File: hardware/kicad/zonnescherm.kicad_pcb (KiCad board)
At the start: 2 copper layers, 75 x 75 mm, 33 parts, among them K1 K1-ON/OFF, K2 K1-UP/DOWN, K3 K2-ON/OFF, K4 K2-UP/DOWN, P1 ARDUINO-ISP, P2 CONN_MAINS, P3 CONN_SUNSHADE1, P4 CONN_SUNSHADE2, P5 SWITCHES, U1 IRM-05-5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

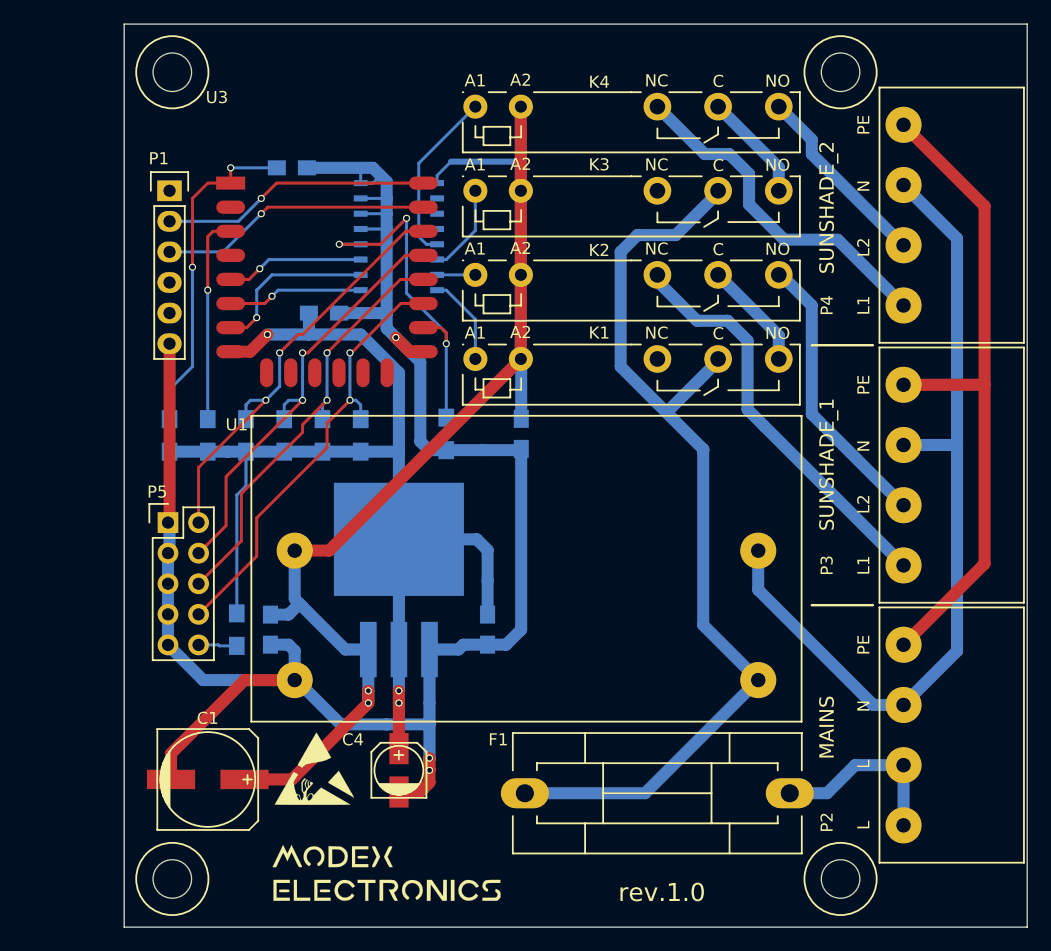
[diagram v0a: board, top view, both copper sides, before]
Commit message: Updated layout with new footprint.
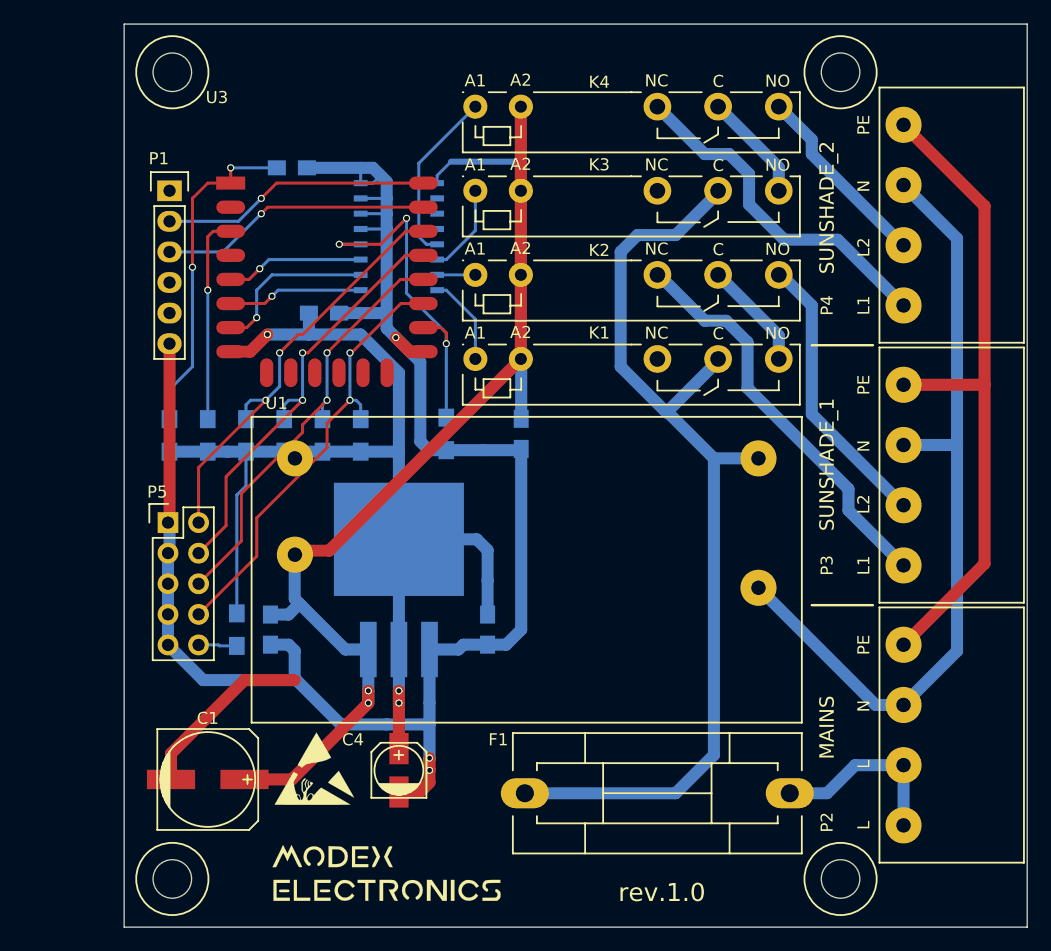
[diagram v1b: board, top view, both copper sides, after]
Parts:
- moved U1 42.7 mm to (122.7, 95.0), turned to 0 degrees
- moved ? 7.37 mm to (153.2, 100.1)
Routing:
- net N: track 70.8 -> 67.6 mm
- net P: track 80.3 -> 82.3 mm

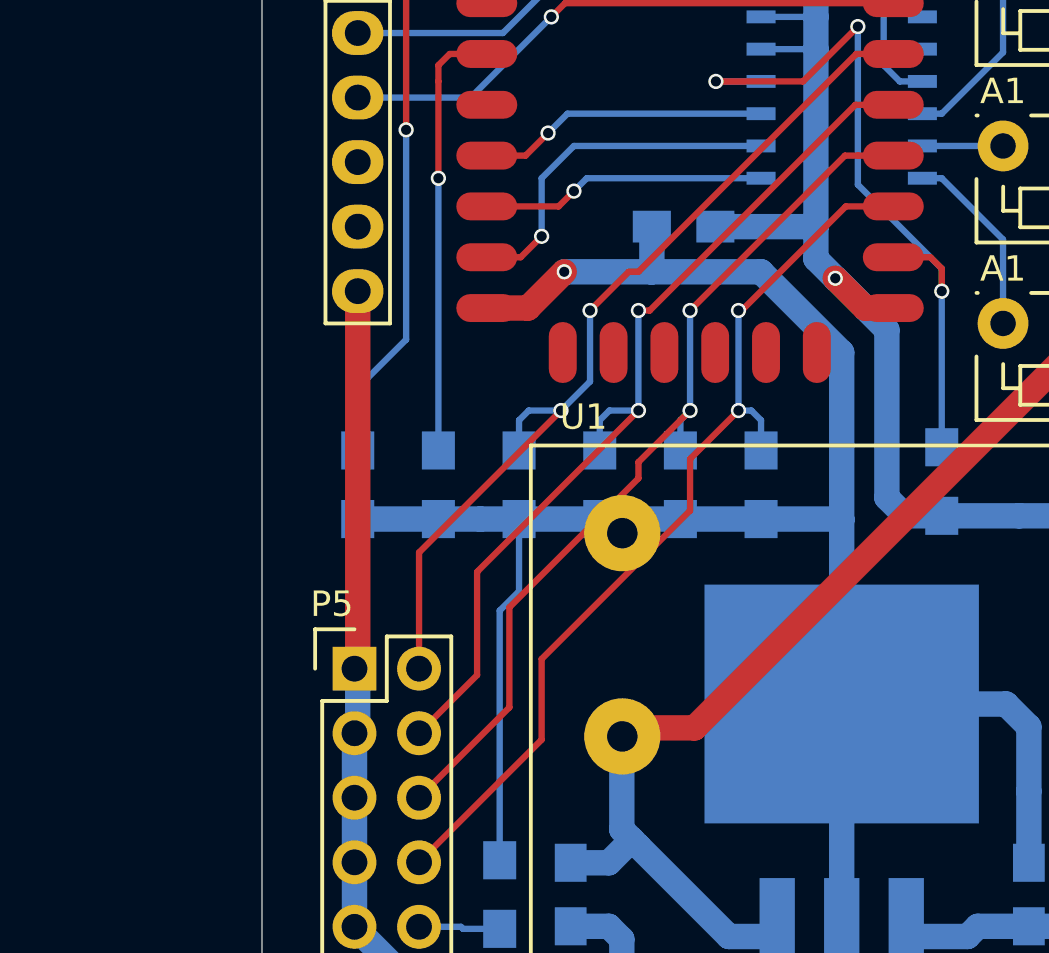
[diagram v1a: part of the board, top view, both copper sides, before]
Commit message: Changed layout of the PCB.
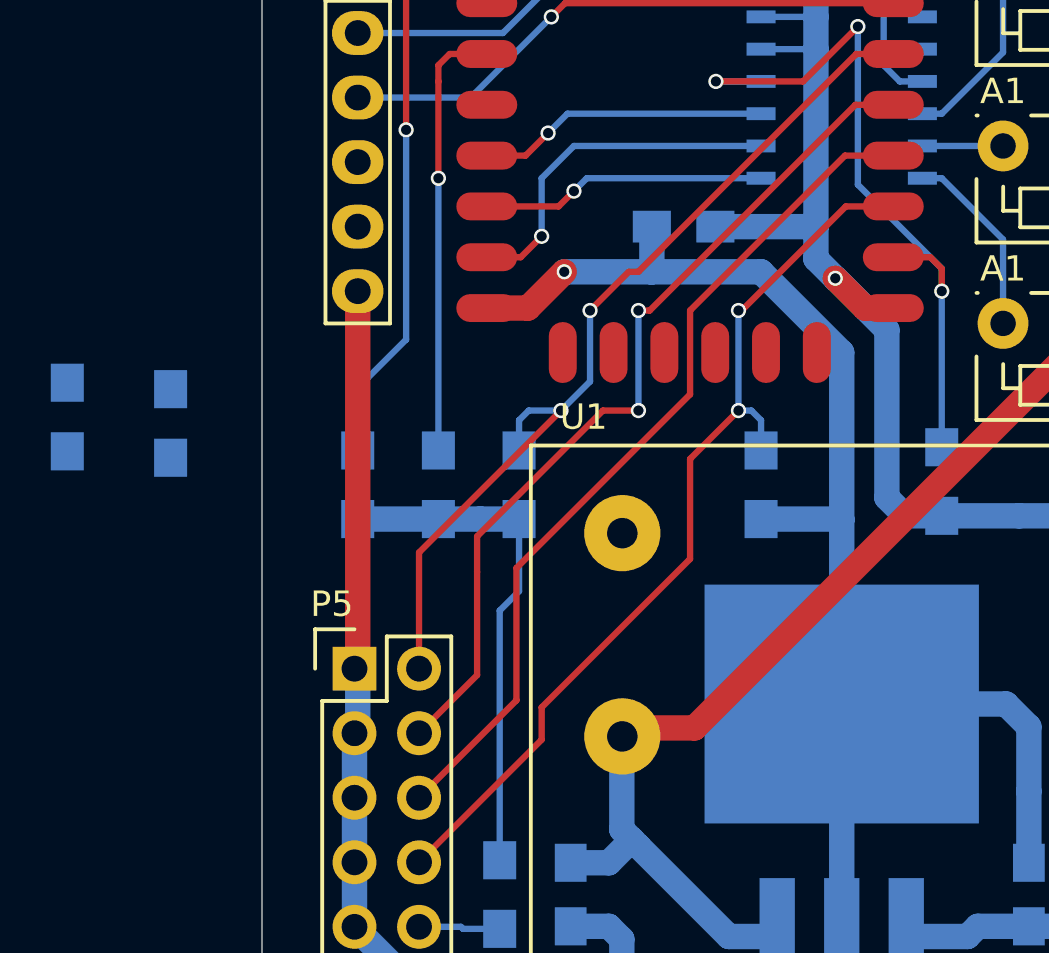
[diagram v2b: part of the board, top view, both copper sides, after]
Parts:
- moved R1 21.1 mm to (100.8, 90.4)
- moved R3 20.2 mm to (104.9, 90.7)
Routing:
- net P3V3: track 104.8 -> 95.3 mm
- net GPIO4: track 36.5 -> 34.4 mm
- net GPIO0: track 35.8 -> 34.1 mm, vias 2 -> 0
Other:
- net class Default: clearance 0.2 -> 0.153; trace_width 0.25 -> 0.2
- rule trace_clearance: 0.2 -> 0.153
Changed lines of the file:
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@@
   (general
     (links 80)
-    (no_connects 2)
+    (no_connects 7)
     (area 108.05 56.953 183.700501 134.128501)
     (thickness 1.6)
     (drawings 18)
-    (tracks 324)
+    (tracks 313)
     (zones 0)
     (modules 33)
@@
   )
   (setup
-    (last_trace_width 1)
+    (last_trace_width 0.2)
     (user_trace_width 0.25)
     (user_trace_width 0.5)
     (user_trace_width 1)
     (user_trace_width 2)
-    (trace_clearance 0.2)
+    (trace_clearance 0.153)
     (zone_clearance 0.508)
     (zone_45_only no)
@@
   (net 46 "Net-(P5-Pad10)")
   (net_class Default "This is the default net class."
-    (clearance 0.2)
-    (trace_width 0.25)
+    (clearance 0.153)
+    (trace_width 0.2)
     (via_dia 0.6)
     (via_drill 0.4)
@@
   )
   (module Resistors_SMD:R_0805_HandSoldering (layer B.Cu)
-    (at 121.793 93.091 90)
+    (at 100.838 90.424 90)
     (descr "Resistor SMD 0805, hand soldering")
     (tags "resistor 0805")
@@
   )
   (module Resistors_SMD:R_0805_HandSoldering (layer B.Cu)
-    (at 124.968 93.091 90)
+    (at 104.902 90.678 90)
     (descr "Resistor SMD 0805, hand soldering")
     (tags "resistor 0805")
@@
   (segment (start 115.443 94.441) (end 117.094 94.441) (width 1) (layer B.Cu) (net 3))
   (segment (start 117.094 94.441) (end 118.618 94.441) (width 1) (layer B.Cu) (net 3))
-  (segment (start 118.618 94.441) (end 121.793 94.441) (width 1) (layer B.Cu) (net 3))
-  (segment (start 121.793 94.441) (end 124.968 94.441) (width 1) (layer B.Cu) (net 3))
-  (segment (start 124.968 94.441) (end 128.143 94.441) (width 1) (layer B.Cu) (net 3))
   (segment (start 131.318 110.871) (end 131.318 101.721) (width 1) (layer B.Cu) (net 3))
   (segment (start 128.143 98.546) (end 131.318 101.721) (width 1) (layer B.Cu) (net 3))
@@
   (segment (start 166.878 122.809) (end 169.211 120.476) (width 1) (layer B.Cu) (net 5))
   (segment (start 157.48 94.996) (end 157.48 119.634) (width 1) (layer B.Cu) (net 6))
-  (segment (start 154.305 122.809) (end 141.78026 122.809) (width 1) (layer B.Cu) (net 6) (status 800000))
+  (segment (start 154.305 122.809) (end 141.78026 122.809) (width 1) (layer B.Cu) (net 6))
   (segment (start 157.48 119.634) (end 154.305 122.809) (width 1) (layer B.Cu) (net 6))
   (segment (start 153.543 91.186) (end 153.67 91.186) (width 1) (layer B.Cu) (net 6))
-  (segment (start 157.48 94.996) (end 161.182 94.996) (width 1) (layer B.Cu) (net 6) (status 800000))
+  (segment (start 157.48 94.996) (end 161.182 94.996) (width 1) (layer B.Cu) (net 6))
   (segment (start 153.67 91.186) (end 157.48 94.996) (width 1) (layer B.Cu) (net 6))
   (segment (start 149.733 87.376) (end 153.543 91.186) (width 1) (layer B.Cu) (net 6))
@@
   (via (at 119.888 74.676) (size 0.6) (drill 0.4) (layers F.Cu B.Cu) (net 9))
   (segment (start 120.428 74.136) (end 119.888 74.676) (width 0.25) (layer F.Cu) (net 9))
-  (segment (start 123.317 90.17) (end 122.174 90.17) (width 0.25) (layer B.Cu) (net 12))
-  (segment (start 121.793 90.551) (end 121.793 91.741) (width 0.25) (layer B.Cu) (net 12))
-  (segment (start 122.174 90.17) (end 121.793 90.551) (width 0.25) (layer B.Cu) (net 12))
+  (segment (start 123.317 90.17) (end 121.92 90.17) (width 0.25) (layer F.Cu) (net 12))
+  (segment (start 116.967 95.123) (end 116.967 96.52) (width 0.25) (layer F.Cu) (net 12))
+  (segment (start 121.92 90.17) (end 116.967 95.123) (width 0.25) (layer F.Cu) (net 12))
   (segment (start 133.348 78.136) (end 131.857 78.136) (width 0.25) (layer F.Cu) (net 12))
   (segment (start 123.317 86.233) (end 123.317 90.17) (width 0.25) (layer B.Cu) (net 12))
@@
   (segment (start 116.967 100.584) (end 114.681 102.87) (width 0.25) (layer F.Cu) (net 12))
   (segment (start 116.967 96.52) (end 116.967 100.584) (width 0.25) (layer F.Cu) (net 12))
-  (segment (start 123.317 90.17) (end 116.967 96.52) (width 0.25) (layer F.Cu) (net 12))
   (via (at 123.317 90.17) (size 0.6) (drill 0.4) (layers F.Cu B.Cu) (net 12))
   (segment (start 121.412 86.233) (end 121.412 89.027) (width 0.25) (layer B.Cu) (net 13))
@@
   (segment (start 120.269 90.17) (end 114.681 95.758) (width 0.25) (layer F.Cu) (net 13))
   (via (at 120.269 90.17) (size 0.6) (drill 0.4) (layers F.Cu B.Cu) (net 13))
-  (segment (start 125.349 90.17) (end 123.317 92.202) (width 0.25) (layer F.Cu) (net 14))
-  (via (at 125.349 90.17) (size 0.6) (drill 0.4) (layers F.Cu B.Cu) (net 14))
-  (segment (start 118.237 101.854) (end 114.681 105.41) (width 0.25) (layer F.Cu) (net 14))
-  (segment (start 118.237 97.917) (end 118.237 101.854) (width 0.25) (layer F.Cu) (net 14))
-  (segment (start 123.317 92.837) (end 118.237 97.917) (width 0.25) (layer F.Cu) (net 14))
-  (segment (start 123.317 92.202) (end 123.317 92.837) (width 0.25) (layer F.Cu) (net 14))
-  (segment (start 125.349 90.17) (end 124.968 90.551) (width 0.25) (layer B.Cu) (net 14))
-  (segment (start 131.954 80.136) (end 131.953 80.137) (width 0.25) (layer F.Cu) (net 14))
-  (segment (start 131.953 80.137) (end 131.445 80.137) (width 0.25) (layer F.Cu) (net 14))
-  (segment (start 131.445 80.137) (end 125.349 86.233) (width 0.25) (layer F.Cu) (net 14))
-  (via (at 125.349 86.233) (size 0.6) (drill 0.4) (layers F.Cu B.Cu) (net 14))
-  (segment (start 125.349 86.233) (end 125.349 90.17) (width 0.25) (layer B.Cu) (net 14))
-  (segment (start 133.348 80.136) (end 131.954 80.136) (width 0.25) (layer F.Cu) (net 14))
-  (segment (start 124.968 90.551) (end 124.968 91.741) (width 0.25) (layer B.Cu) (net 14))
+  (segment (start 133.348 80.136) (end 131.446 80.136) (width 0.25) (layer F.Cu) (net 14))
+  (segment (start 118.5164 101.5746) (end 114.681 105.41) (width 0.25) (layer F.Cu) (net 14))
+  (segment (start 118.5164 96.3676) (end 118.5164 101.5746) (width 0.25) (layer F.Cu) (net 14))
+  (segment (start 125.349 89.535) (end 118.5164 96.3676) (width 0.25) (layer F.Cu) (net 14))
+  (segment (start 125.349 86.233) (end 125.349 89.535) (width 0.25) (layer F.Cu) (net 14))
+  (segment (start 131.446 80.136) (end 125.349 86.233) (width 0.25) (layer F.Cu) (net 14))
+  (segment (start 125.349 92.1004) (end 125.349 96.012) (width 0.25) (layer F.Cu) (net 15))
+  (segment (start 125.349 96.012) (end 119.507 101.854) (width 0.25) (layer F.Cu) (net 15))
   (segment (start 127.254 90.17) (end 127.762 90.17) (width 0.25) (layer B.Cu) (net 15))
   (segment (start 127.762 90.17) (end 128.143 90.551) (width 0.25) (layer B.Cu) (net 15))
   (segment (start 133.348 82.136) (end 131.478 82.136) (width 0.25) (layer F.Cu) (net 15))
-  (segment (start 125.349 92.075) (end 125.349 94.107) (width 0.25) (layer F.Cu) (net 15))
+  (segment (start 125.349 92.075) (end 125.349 92.1004) (width 0.25) (layer F.Cu) (net 15))
   (segment (start 127.254 90.17) (end 125.349 92.075) (width 0.25) (layer F.Cu) (net 15))
   (via (at 127.254 90.17) (size 0.6) (drill 0.4) (layers F.Cu B.Cu) (net 15))
@@
   (segment (start 128.143 91.741) (end 128.143 90.551) (width 0.25) (layer B.Cu) (net 15))
   (segment (start 119.507 103.124) (end 114.681 107.95) (width 0.25) (layer F.Cu) (net 15))
-  (segment (start 119.507 99.949) (end 119.507 103.124) (width 0.25) (layer F.Cu) (net 15))
-  (segment (start 125.349 94.107) (end 119.507 99.949) (width 0.25) (layer F.Cu) (net 15))
+  (segment (start 119.507 101.854) (end 119.507 103.124) (width 0.25) (layer F.Cu) (net 15))
   (segment (start 115.443 91.741) (end 115.443 81.026) (width 0.25) (layer B.Cu) (net 16))
   (segment (start 115.888 76.136) (end 117.348 76.136) (width 0.25) (layer F.Cu) (net 16))
@@
   (segment (start 165.608 82.296) (end 163.068 79.756) (width 1) (layer B.Cu) (net 38))
   (segment (start 162.868 79.756) (end 163.068 79.756) (width 0.25) (layer B.Cu) (net 38))
-  (segment (start 152.788 79.756) (end 152.908 79.756) (width 1) (layer B.Cu) (net 39) (status C00000))
-  (segment (start 152.908 79.756) (end 156.718 83.566) (width 1) (layer B.Cu) (net 39) (status 400000))
-  (segment (start 168.656 99.312) (end 173.23 103.886) (width 1) (layer B.Cu) (net 39) (status 800000))
+  (segment (start 152.788 79.756) (end 152.908 79.756) (width 1) (layer B.Cu) (net 39))
+  (segment (start 152.908 79.756) (end 156.718 83.566) (width 1) (layer B.Cu) (net 39))
+  (segment (start 168.656 99.312) (end 173.23 103.886) (width 1) (layer B.Cu) (net 39))
   (segment (start 168.656 97.536) (end 168.656 99.312) (width 1) (layer B.Cu) (net 39))
   (segment (start 160.274 89.154) (end 168.656 97.536) (width 1) (layer B.Cu) (net 39))
